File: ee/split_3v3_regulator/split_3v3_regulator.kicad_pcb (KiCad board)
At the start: 2 copper layers, 11 parts, among them J1 Conn_01x04, J2 Conn_01x04, J3 Conn_01x02, U1 TPS62120

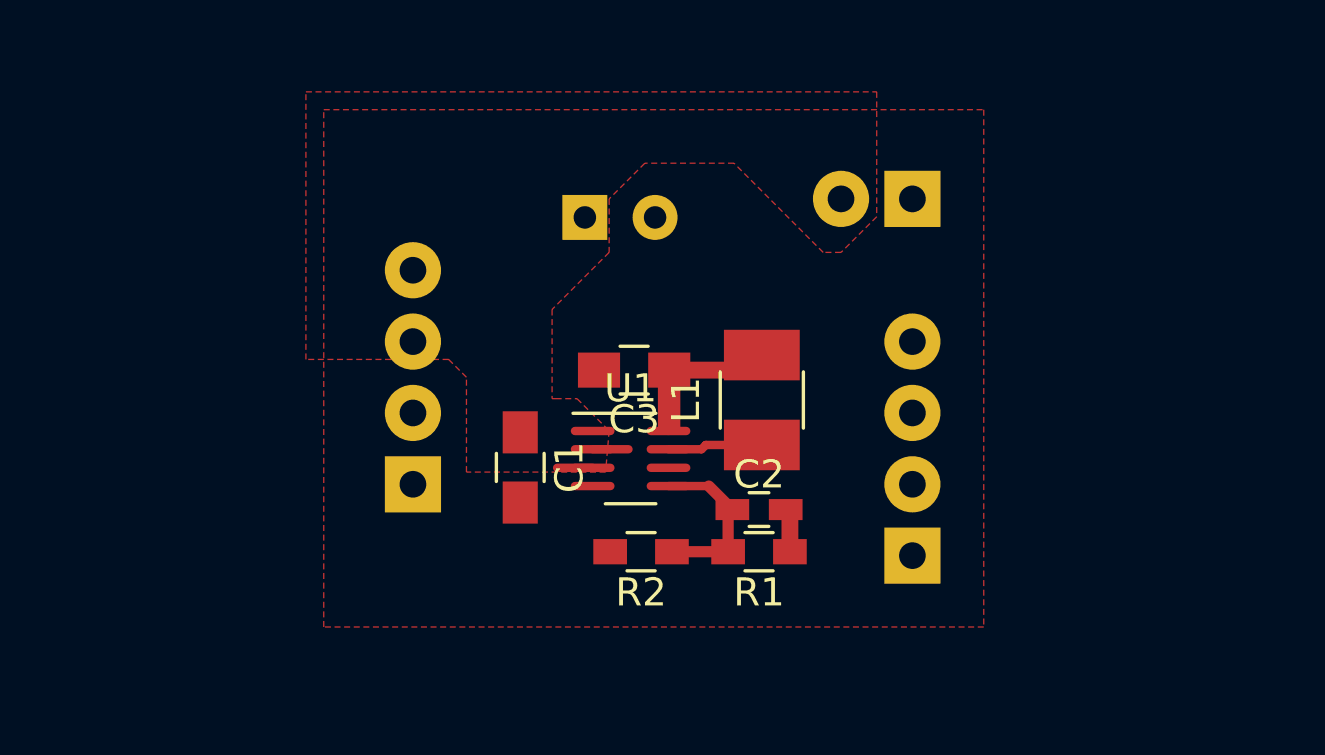
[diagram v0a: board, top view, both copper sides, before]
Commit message: finished rev1 of 3v3 regulator board
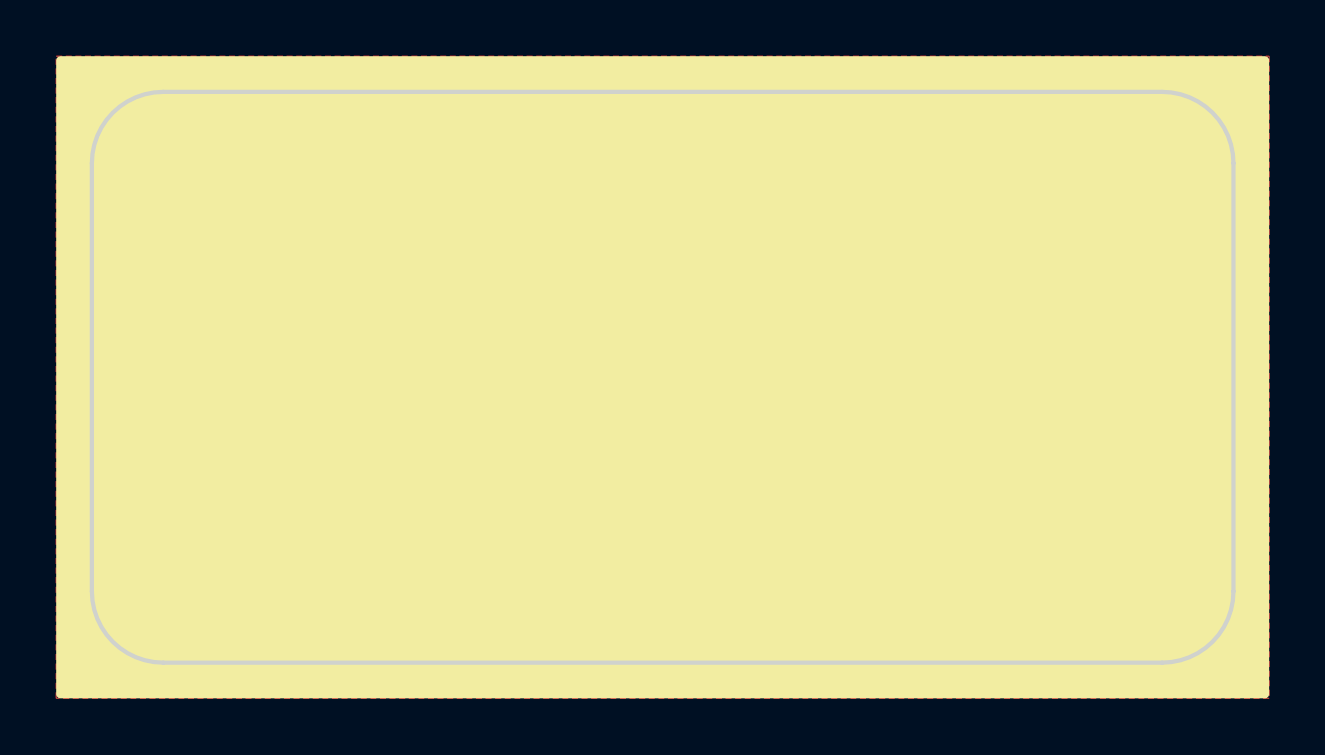
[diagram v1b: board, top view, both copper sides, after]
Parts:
- J2: value Conn_01x04 -> Conn_01x02; footprint Connectors_Samtec:SL-104-X-XX_1x04 -> Connectors_Samtec:SL-102-X-XX_1x02; moved to F.Cu
- moved J2 2.54 mm to (137.2, 114.3)
- moved J3 2.54 mm to (137.2, 106.7), turned to 0 degrees
- moved C4 0.91 mm to (126.2, 104.3), turned to 270 degrees
- moved C1 0.35 mm to (123.2, 114.0)
- moved C3 0.14 mm to (127.3, 110.1)
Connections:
- J2 pad 2: GND -> /Vout
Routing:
- net /Vout: track 10.4 -> 3.51 mm
- net +12V: track 1.27 -> 4.70 mm
- added copper zone on F.Cu, net /Vout
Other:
- board outline added: 40.6 x 20.3 mm
- net class Default: trace_width 0.6 -> 0.38
- board text added: "12 V"
- board text added: "3.3 V"
- board text added: "GND"

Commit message: flip 12V output connector to match carrier board
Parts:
- moved J1 7.62 mm to (119.4, 106.7), turned to 180 degrees
- moved J3 2.54 mm to (137.2, 104.1), turned to 180 degrees
- moved C4 2.39 mm to (125.2, 106.4), turned to 90 degrees
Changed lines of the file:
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@@
     (visible_elements 7FFFFF9F)
     (pcbplotparams
-      (layerselection 0x00820_00000001)
+      (layerselection 0x01000_00000001)
       (usegerberextensions false)
       (excludeedgelayer true)
@@
   )
   (module Connectors_Samtec:SL-102-X-XX_1x02 (layer B.Cu)
-    (at 137.16 106.68)
+    (at 137.16 104.14 180)
     (descr "Low profile, screw machine socket strip, through hole, 100mil / 2.54mm pitch")
     (tags "samtec socket strip tht single")
-    (fp_text reference J3 (at -2.27 -1.27 270) (layer B.SilkS)
-      (effects (font (size 1 1) (thickness 0.15)) (justify mirror))
-    )
-    (fp_text value Conn_01x02 (at 2.27 -1.27 270) (layer B.Fab)
+    (fp_text reference J3 (at -2.27 -1.27 450) (layer B.SilkS)
+      (effects (font (size 1 1) (thickness 0.15)) (justify mirror))
+    )
+    (fp_text value Conn_01x02 (at 2.27 -1.27 450) (layer B.Fab)
       (effects (font (size 1 1) (thickness 0.15)) (justify mirror))
     )
@@
     (fp_line (start -1.27 -3.81) (end -1.07 -3.81) (layer B.Fab) (width 0.1))
     (fp_line (start 1.27 -3.81) (end 1.07 -3.81) (layer B.Fab) (width 0.1))
-    (fp_text user %R (at 0 -1.27 270) (layer B.Fab)
-      (effects (font (size 1 1) (thickness 0.15)) (justify mirror))
-    )
-    (pad 1 thru_hole rect (at 0 0) (size 2 2) (drill 0.95) (layers *.Cu *.Mask)
-      (net 2 GND))
-    (pad 2 thru_hole circle (at 0 -2.54) (size 2 2) (drill 0.95) (layers *.Cu *.Mask)
+    (fp_text user %R (at 0 -1.27 450) (layer B.Fab)
+      (effects (font (size 1 1) (thickness 0.15)) (justify mirror))
+    )
+    (pad 1 thru_hole rect (at 0 0 180) (size 2 2) (drill 0.95) (layers *.Cu *.Mask)
+      (net 2 GND))
+    (pad 2 thru_hole circle (at 0 -2.54 180) (size 2 2) (drill 0.95) (layers *.Cu *.Mask)
       (net 1 +12V))
     (model ${KISYS3DMOD}/Connectors_Samtec.3dshapes/SL-102-X-XX_1x02.wrl
@@
   )
   (module Capacitors_THT:CP_Radial_D6.3mm_P2.50mm (layer B.Cu)
-    (at 126.238 104.267 270)
+    (at 125.222 106.426 90)
     (descr "CP, Radial series, Radial, pin pitch=2.50mm, , diameter=6.3mm, Electrolytic Capacitor")
     (tags "CP Radial series Radial pin pitch 2.50mm  diameter 6.3mm Electrolytic Capacitor")
-    (fp_text reference C4 (at 1.25 4.46 270) (layer B.SilkS)
-      (effects (font (size 1 1) (thickness 0.15)) (justify mirror))
-    )
-    (fp_text value 100u (at 1.25 -4.46 270) (layer B.Fab)
+    (fp_text reference C4 (at 1.25 4.46 90) (layer B.SilkS)
+      (effects (font (size 1 1) (thickness 0.15)) (justify mirror))
+    )
+    (fp_text value 100u (at 1.25 -4.46 90) (layer B.Fab)
       (effects (font (size 1 1) (thickness 0.15)) (justify mirror))
     )
@@
     (fp_line (start 4.75 -3.5) (end 4.75 3.5) (layer B.CrtYd) (width 0.05))
     (fp_line (start 4.75 3.5) (end -2.25 3.5) (layer B.CrtYd) (width 0.05))
-    (fp_text user %R (at 1.25 0 270) (layer B.Fab)
-      (effects (font (size 1 1) (thickness 0.15)) (justify mirror))
-    )
-    (pad 1 thru_hole rect (at 0 0 270) (size 1.6 1.6) (drill 0.8) (layers *.Cu *.Mask)
+    (fp_text user %R (at 1.25 0 90) (layer B.Fab)
+      (effects (font (size 1 1) (thickness 0.15)) (justify mirror))
+    )
+    (pad 1 thru_hole rect (at 0 0 90) (size 1.6 1.6) (drill 0.8) (layers *.Cu *.Mask)
       (net 1 +12V))
-    (pad 2 thru_hole circle (at 2.5 0 270) (size 1.6 1.6) (drill 0.8) (layers *.Cu *.Mask)
+    (pad 2 thru_hole circle (at 2.5 0 90) (size 1.6 1.6) (drill 0.8) (layers *.Cu *.Mask)
       (net 2 GND))
     (model ${KISYS3DMOD}/Capacitors_THT.3dshapes/CP_Radial_D6.3mm_P2.50mm.wrl
@@
   )
   (module Connectors_Samtec:SL-104-X-XX_1x04 (layer B.Cu)
-    (at 119.38 114.3)
+    (at 119.38 106.68 180)
     (descr "Low profile, screw machine socket strip, through hole, 100mil / 2.54mm pitch")
     (tags "samtec socket strip tht single")
-    (fp_text reference J1 (at -2.27 -3.81 270) (layer B.SilkS)
-      (effects (font (size 1 1) (thickness 0.15)) (justify mirror))
-    )
-    (fp_text value Conn_01x04 (at 2.27 -3.81 270) (layer B.Fab)
+    (fp_text reference J1 (at -2.27 -3.81 450) (layer B.SilkS)
+      (effects (font (size 1 1) (thickness 0.15)) (justify mirror))
+    )
+    (fp_text value Conn_01x04 (at 2.27 -3.81 450) (layer B.Fab)
       (effects (font (size 1 1) (thickness 0.15)) (justify mirror))
     )
@@
     (fp_line (start -1.27 -8.89) (end -1.07 -8.89) (layer B.Fab) (width 0.1))
     (fp_line (start 1.27 -8.89) (end 1.07 -8.89) (layer B.Fab) (width 0.1))
-    (fp_text user %R (at 0 -3.81 270) (layer B.Fab)
-      (effects (font (size 1 1) (thickness 0.15)) (justify mirror))
-    )
-    (pad 1 thru_hole rect (at 0 0) (size 2 2) (drill 0.95) (layers *.Cu *.Mask)
-      (net 2 GND))
-    (pad 2 thru_hole circle (at 0 -2.54 315) (size 2 2) (drill 0.95) (layers *.Cu *.Mask)
-      (net 2 GND))
-    (pad 3 thru_hole circle (at 0 -5.08 315) (size 2 2) (drill 0.95) (layers *.Cu *.Mask)
+    (fp_text user %R (at 0 -3.81 450) (layer B.Fab)
+      (effects (font (size 1 1) (thickness 0.15)) (justify mirror))
+    )
+    (pad 1 thru_hole rect (at 0 0 180) (size 2 2) (drill 0.95) (layers *.Cu *.Mask)
+      (net 2 GND))
+    (pad 2 thru_hole circle (at 0 -2.54 135) (size 2 2) (drill 0.95) (layers *.Cu *.Mask)
+      (net 2 GND))
+    (pad 3 thru_hole circle (at 0 -5.08 135) (size 2 2) (drill 0.95) (layers *.Cu *.Mask)
       (net 1 +12V))
-    (pad 4 thru_hole circle (at 0 -7.62 315) (size 2 2) (drill 0.95) (layers *.Cu *.Mask)
+    (pad 4 thru_hole circle (at 0 -7.62 135) (size 2 2) (drill 0.95) (layers *.Cu *.Mask)
       (net 1 +12V))
     (model ${KISYS3DMOD}/Connectors_Samtec.3dshapes/SL-104-X-XX_1x04.wrl
@@
   (gr_line (start 115.316 105.664) (end 115.316 110.236) (angle 90) (layer Eco2.User) (width 0.2))
   (gr_line (start 115.316 110.744) (end 115.316 115.316) (angle 90) (layer Eco2.User) (width 0.2))
-  (gr_text GND (at 114.3 115.57) (layer Eco2.User)
+  (gr_text GND (at 114.3 105.41) (layer Eco2.User)
     (effects (font (size 1.5 1.5) (thickness 0.25)) (justify right))
   )
-  (gr_text "12 V" (at 114.3 105.41) (layer Eco2.User)
+  (gr_text "12 V" (at 114.3 115.57) (layer Eco2.User)
     (effects (font (size 1.5 1.5) (thickness 0.3)) (justify right))
   )
@@
     (effects (font (size 1.5 1.5) (thickness 0.25)) (justify left))
   )
-  (gr_text GND (at 140.97 107.95) (layer Eco2.User)
+  (gr_text GND (at 140.97 102.87) (layer Eco2.User)
     (effects (font (size 1.5 1.5) (thickness 0.25)) (justify left))
   )
-  (gr_text "12 V" (at 140.97 102.87) (layer Eco2.User)
+  (gr_text "12 V" (at 140.97 107.95) (layer Eco2.User)
     (effects (font (size 1.5 1.5) (thickness 0.3)) (justify left))
   )
@@
     (polygon
       (pts
-        (xy 118.11 110.109) (xy 120.904 110.109) (xy 120.904 111.379) (xy 118.11 111.379)
+        (xy 117.983 110.109) (xy 120.777 110.109) (xy 120.777 110.998) (xy 117.983 110.998)
       )
     )
@@
     )
   )
-  (zone (net 1) (net_name +12V) (layer F.Cu) (hatch edge 0.508)
-    (priority 4)
-    (connect_pads (clearance 0.3))
-    (min_thickness 0.3)
-    (fill yes (arc_segments 16) (thermal_gap 0.3) (thermal_bridge_width 0.4) (smoothing fillet) (radius 0.5))
-    (polygon
-      (pts
-        (xy 117.602 102.362) (xy 138.938 102.362) (xy 138.938 105.41) (xy 131.445 105.41) (xy 124.425 105.41)
-        (xy 124.425 112.21) (xy 125.765 112.21) (xy 125.765 113.925) (xy 121.285 113.925) (xy 121.285 109.728)
-        (xy 117.602 109.728)
-      )
-    )
-  )
   (zone (net 0) (net_name "") (layer F.Cu) (hatch edge 0.508)
     (connect_pads (clearance 0.3))
@@
       )
     )
+  )
+  (zone (net 1) (net_name +12V) (layer F.Cu) (hatch edge 0.508)
+    (priority 4)
+    (connect_pads (clearance 0.3))
+    (min_thickness 0.3)
+    (fill yes (arc_segments 16) (thermal_gap 0.3) (thermal_bridge_width 0.4) (smoothing fillet) (radius 0.5))
+    (polygon
+      (pts
+        (xy 138.938 108.458) (xy 136.398 108.458) (xy 135.128 107.188) (xy 127 107.188) (xy 125.984 108.204)
+        (xy 124.46 108.204) (xy 124.206 108.458) (xy 124.206 111.252) (xy 124.968 112.014) (xy 125.73 112.014)
+        (xy 125.73 113.792) (xy 121.158 113.792) (xy 121.158 116.078) (xy 117.602 116.078) (xy 117.602 110.49)
+        (xy 120.65 110.49) (xy 122.428 108.712) (xy 122.428 105.41) (xy 138.938 105.41)
+      )
+    )
+  )
+  (zone (net 0) (net_name "") (layer F.Cu) (hatch edge 0.508)
+    (connect_pads (clearance 0.3))
+    (min_thickness 0.3)
+    (keepout (tracks not_allowed) (vias not_allowed) (copperpour not_allowed))
+    (fill (arc_segments 16) (thermal_gap 0.3) (thermal_bridge_width 0.4))
+    (polygon
+      (pts
+        (xy 127.762 110.998) (xy 126.746 110.998) (xy 126.746 109.22) (xy 127.762 109.22)
+      )
+    )

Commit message: swap 12V input and 3V3 output headers
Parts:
- moved J2 10.2 mm to (137.2, 104.1)
- moved J3 10.2 mm to (137.2, 114.3)
- moved C4 8.70 mm to (126.2, 115.1), turned to 270 degrees
- moved C1 7.37 mm to (123.2, 106.7), turned to 90 degrees
- moved C2 5.08 mm to (131.7, 110.1)
- moved C3 5.08 mm to (127.3, 105.0)
- moved L1 5.08 mm to (131.8, 106.2)
- moved R1 5.08 mm to (131.7, 111.6)
- moved R2 5.08 mm to (127.5, 111.6)
- moved U1 5.08 mm to (127.1, 108.3)
